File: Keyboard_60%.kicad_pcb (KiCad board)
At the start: 2 copper layers, 284.7 x 94.2 mm, 207 parts, among them J1 JST-4-pin, J3 Prog_conn, J4 TYPE-C-31-M12_13, J5 Tag connect TC2030-CTX, SW1 MK-12C02-G025, SW2 Reset Switch, U1 BQ24074RGTR, U3 nRF52840-QIAA-R/nRF52833-QIAA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, U4 TPD4E05U06DQAR, Y1 32MHz, Y2 32.768kHz

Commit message: Added mounting holes for tray mount style
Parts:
- added H3: MountingHole, keyboard:salvation_mounting_holes, F.Cu at (127.2, 111.3)
- added H4: MountingHole, keyboard:salvation_mounting_holes, F.Cu at (128.3, 117.5)
- added H5: MountingHole, keyboard:PKRHSL, F.Cu at (0.65, 56.5)
- added H6: MountingHole, keyboard:PKRHSL, F.Cu at (284.0, 56.5)
- moved D38 7.05 mm to (135.1, 51.8)
- moved D62 4.67 mm to (195.4, 80.5), turned to 0 degrees
- moved J3 1.49 mm to (3.83, 67.1)
- moved L4 0.64 mm to (29.6, 31.9), turned to 0 degrees
- moved MX36 0.14 mm to (102.7, 42.6)
- moved MX35 0.12 mm to (83.6, 42.6)
- moved MX37 0.07 mm to (121.7, 42.6)
- moved MX34 0.07 mm to (64.5, 42.6)
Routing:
- net /switch_matrix/ROW4: track 274.5 -> 280.7 mm
- net /~{nReset}: track 101.7 -> 106.4 mm, vias 8 -> 11
- net /DB_SWO: track 25.5 -> 28.6 mm
- net Net-(U3-DEC4): track 36.0 -> 33.8 mm
- net /switch_matrix/ROW2: track 285.1 -> 283.2 mm
- net Net-(D62-A): track 5.01 -> 3.94 mm
- net /DB_SWDCLK: track 22.0 -> 23.1 mm, vias 1 -> 2
- net Net-(D38-A): track 4.30 -> 5.29 mm
- net /DB_SWDIO: track 19.0 -> 18.8 mm, vias 1 -> 0

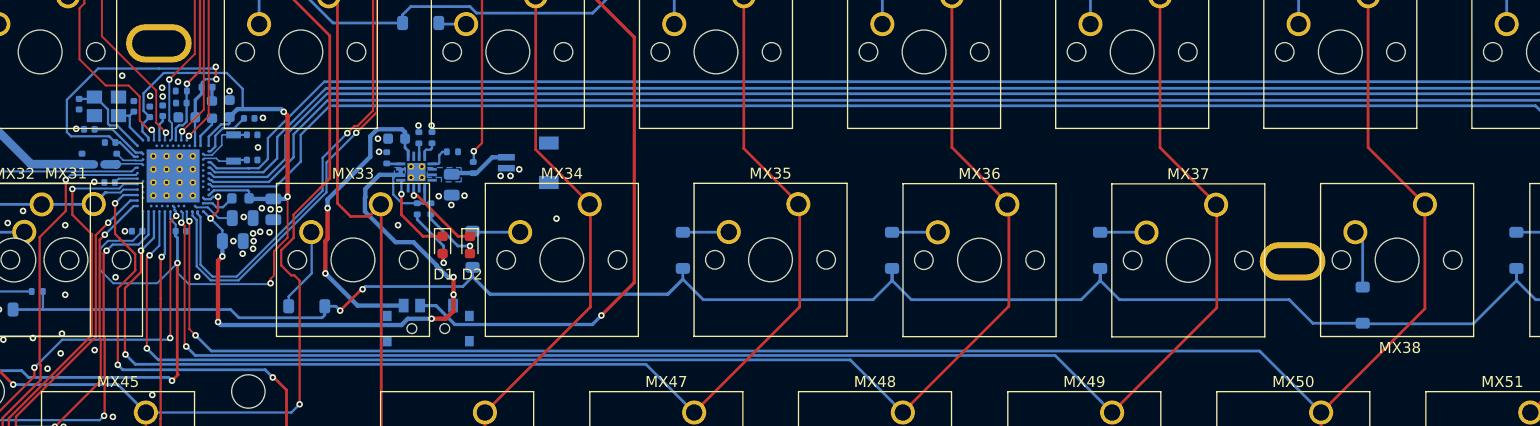
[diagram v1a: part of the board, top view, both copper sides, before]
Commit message: Added Keryboard name credits, guard rings for crystals and Keyboard name in soldermask layer
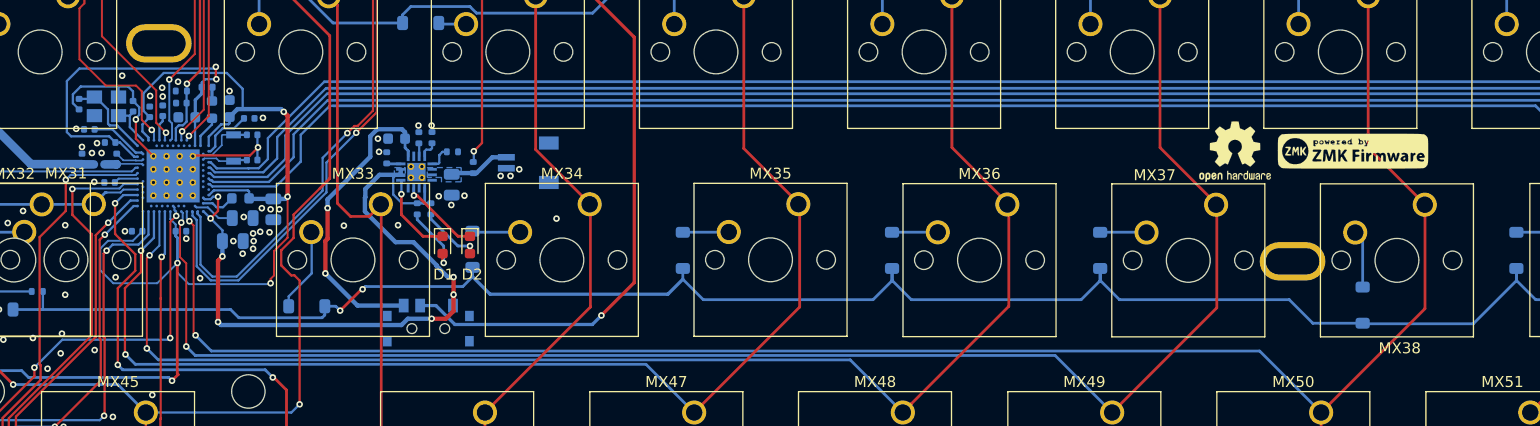
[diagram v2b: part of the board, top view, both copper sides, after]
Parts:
- added G***: LOGO, keyboard:ZMK_logo, F.Cu at (134.2, 37.7)
- added REF**: OSHW-Logo, keyboard:OSHW-Logo, F.Cu at (123.5, 37.8)
- moved C5 0.08 mm to (22.8, 33.6)
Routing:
- net GND: track 0.03 -> 24.1 mm, vias 67 -> 74
- net Net-(U3-DEC4): track 33.8 -> 34.8 mm
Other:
- board text added: "Name Credits : VK"
- board text added: "TR-60"

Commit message: Made space for salvation case supporters on back layer
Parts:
- moved D59 19.9 mm to (46.1, 84.8)
- moved D5 16.1 mm to (55.5, 9.32)
- moved D12 16.0 mm to (188.4, 9.30)
- moved D9 15.9 mm to (131.3, 9.30)
- moved R23 2.24 mm to (21.7, 85.5)
- moved D17 0.91 mm to (271.4, 12.7)
- moved D16 0.67 mm to (249.5, 9.00)
- moved D65 0.51 mm to (263.8, 84.9)
- moved D4 0.44 mm to (36.0, 9.30)
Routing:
- net Net-(D12-A): track 5.45 -> 12.8 mm
- net Net-(D9-A): track 5.31 -> 12.6 mm
- net /switch_matrix/ROW0: track 276.6 -> 283.4 mm
- net Net-(D5-A): track 5.21 -> 12.0 mm
- net Net-(D59-A): track 8.24 -> 14.2 mm
- net /switch_matrix/ROW4: track 280.7 -> 286.3 mm
- net /ROW4: track 64.9 -> 62.9 mm
- net Net-(D16-A): track 5.81 -> 5.03 mm
- net Net-(D4-A): track 12.5 -> 11.7 mm
- net /COL13: track 368.0 -> 367.3 mm
- net Net-(D17-A): track 16.5 -> 15.9 mm
- net Net-(D65-A): track 6.83 -> 6.29 mm

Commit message: Generated production files for PCB
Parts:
- added G***: LOGO, keyboard:BLE-symbol, F.Cu at (147.6, 39.7)
- added L6: 2.2nH, keyboard:L_0402_1005Metric, B.Cu at (16.7, 38.9)
- C10: value 0.8pF -> 1pF
- C11: value 0.5pF -> 1.2pF
- moved G*** 2.00 mm to (136.2, 38.0)
- moved REF** 0.39 mm to (123.5, 37.4)
- moved MX16 0.06 mm to (269.2, 4.50)
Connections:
- C11 pad 1: /ANT_FEED -> Net-(C11-Pad1)
- L1 pad 2: /ANT_FEED -> Net-(C11-Pad1)
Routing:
- net /ANT_FEED: track 14.7 -> 11.6 mm
- net Net-(C11-Pad1): track 0.00 -> 2.12 mm
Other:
- board text added: "BLE"
- board text added: "Enabled"
- board text added: "Logo Credits : VK"
- board text removed: "Name Credits : VK"
